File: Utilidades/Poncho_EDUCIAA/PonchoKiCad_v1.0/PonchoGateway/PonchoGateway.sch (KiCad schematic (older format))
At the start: 6 parts, among them SW1 SW_Push

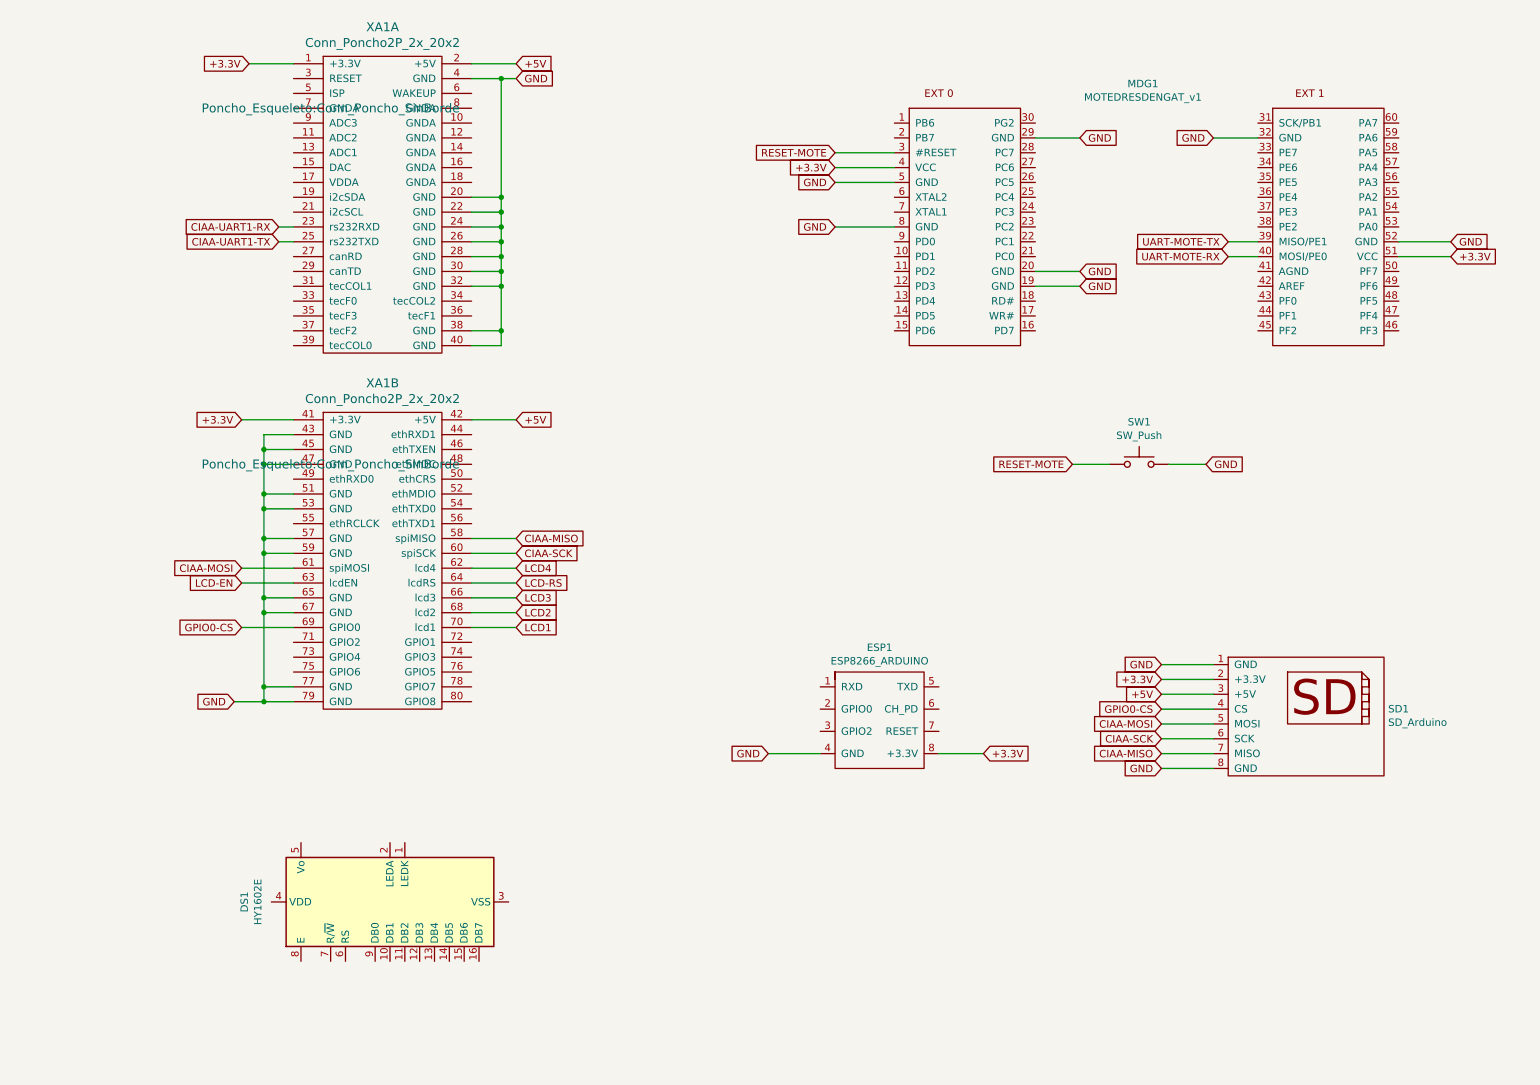
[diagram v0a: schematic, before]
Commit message: Arreglo PonchoGateway, corrijo huellas y ubico componentes en la placa final.
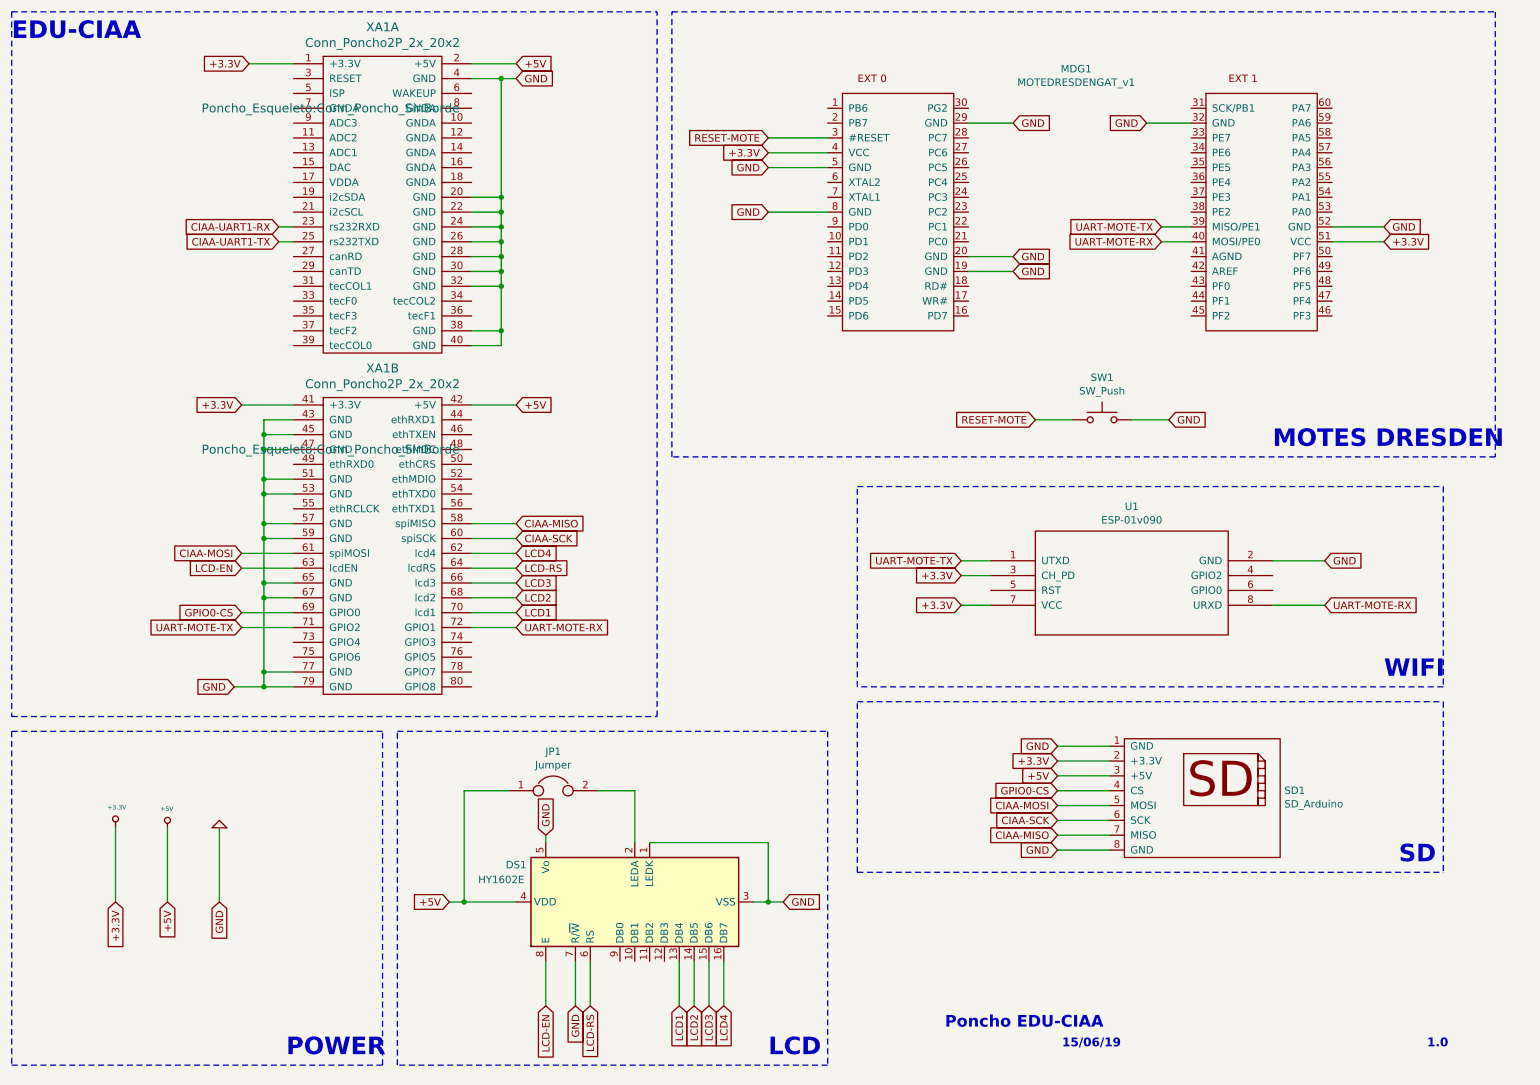
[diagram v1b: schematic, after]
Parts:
- removed ESP1: ESP8266_ARDUINO, symbol LibreriaPropia:ESP8266_ARDUINO
- added JP1: Jumper, lib-ESP8266:JUMPER-PONCHO-EDU-CIAA, symbol Device:Jumper
- added U1: ESP-01v090, lib-ESP8266:ESP-01, symbol ESP8266:ESP-01v090
- DS1: footprint Display:HY1602E -> Display:Display_Propio
- MDG1: footprint (none) -> Connector_Samtec_HLE_SMD:SAMTEC-EDU-CIAA
- SD1: footprint (none) -> lib-ESP8266:SD-SHIELD-ARD
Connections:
- net +3.3V: now also U1.3 (CH_PD), U1.7 (VCC)
- net +5V: now also DS1.4 (VDD), JP1.1
- net GND: now also DS1.1 (LEDK), DS1.3 (VSS), DS1.5 (Vo), DS1.7 (R/~W), U1.2 (GND)
- net LCD-EN: now also DS1.8 (E)
- net LCD-RS: now also DS1.6 (RS)
- net LCD1: now also DS1.13 (DB4)
- net LCD2: now also DS1.14 (DB5)
- net LCD3: now also DS1.15 (DB6)
- net LCD4: now also DS1.16 (DB7)
- net UART-MOTE-RX: now also XA1.72 (GPIO1), U1.8 (URXD)
- net UART-MOTE-TX: now also XA1.71 (GPIO2), U1.1 (UTXD)
- net at DS1.2 (LEDA): now also JP1.2
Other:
- note added: "1.0"
- note added: "15/06/19"
- note added: "EDU-CIAA"
- note added: "LCD"
- note added: "MOTES DRESDEN\n"
- note added: "POWER"
- note added: "Poncho EDU-CIAA"
- note added: "SD"
- note added: "WIFI"
- moved on the sheet: DS1, MDG1, SD1, SW1, XA1B

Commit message: Se corrige error en esquemático, y se termina el pcb.
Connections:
- net CIAA-UART1-RX: now also U1.1 (UTXD)
- net CIAA-UART1-TX: now also U1.8 (URXD)
- net UART-MOTE-RX: no longer U1.8 (URXD)
- net UART-MOTE-TX: no longer U1.1 (UTXD)
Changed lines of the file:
@@
 Text Notes 8130 7640 0    59   ~ 12
 15/06/19
+Text GLabel 9900 4350 2    50   Input ~ 0
+GND
+Wire Wire Line
+	9550 4350 9900 4350
+Text GLabel 7450 4450 0    50   Input ~ 0
++3.3V
+Text GLabel 7450 4650 0    50   Input ~ 0
++3.3V
+Wire Wire Line
+	7650 4450 7450 4450
+Wire Wire Line
+	7650 4650 7450 4650
+Text GLabel 7450 4350 0    50   Input ~ 0
+CIAA-UART1-RX
 $Comp
 L ESP8266:ESP-01v090 U1
@@
 	1    0    0    -1
 $EndComp
-Text GLabel 7450 4350 0    50   Input ~ 0
-UART-MOTE-TX
 Wire Wire Line
-	7450 4350 7650 4350
-Text GLabel 9900 4350 2    50   Input ~ 0
-GND
-Wire Wire Line
-	9550 4350 9900 4350
+	7650 4350 7450 4350
 Text GLabel 9900 4650 2    50   Input ~ 0
-UART-MOTE-RX
+CIAA-UART1-TX
 Wire Wire Line
 	9900 4650 9550 4650
-Text GLabel 7450 4450 0    50   Input ~ 0
-+3.3V
-Text GLabel 7450 4650 0    50   Input ~ 0
-+3.3V
-Wire Wire Line
-	7650 4450 7450 4450
-Wire Wire Line
-	7650 4650 7450 4650
 $EndSCHEMATC

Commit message: Se corrigen problemas en el SCH y PCB. Se realiza última comprobación antes de hacer la placa.
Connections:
- net GND: now also MDG1.41 (AGND)
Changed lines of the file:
@@
 Wire Wire Line
 	9900 4650 9550 4650
+Text GLabel 8800 2300 0    50   Input ~ 0
+GND
+Wire Wire Line
+	9000 2300 8800 2300
 $EndSCHEMATC
